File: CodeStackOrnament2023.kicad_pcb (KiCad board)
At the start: 2 copper layers, 68.8 x 68.8 mm, 26 parts, among them SW1 SW_SPST, U1 TLC555xD, U2 74VHC4040FT

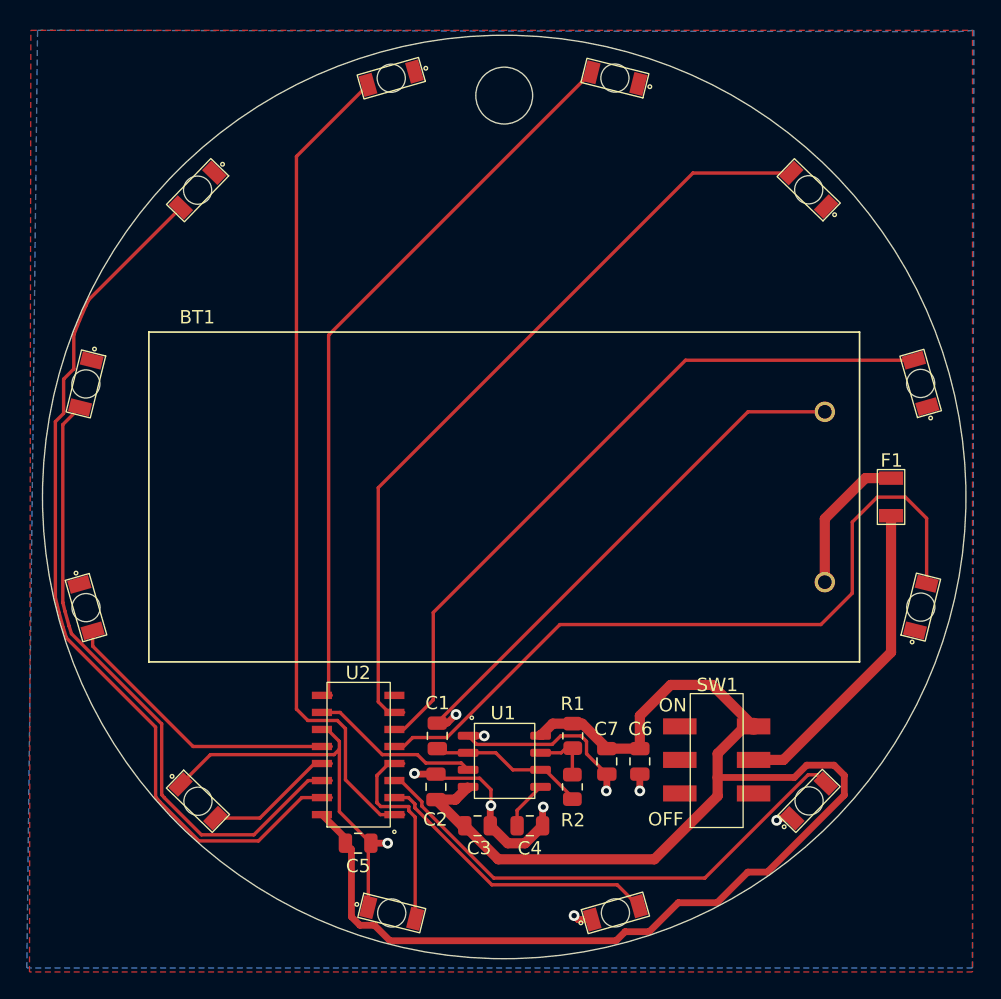
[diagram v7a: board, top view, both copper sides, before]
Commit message: increasing board size a bit.
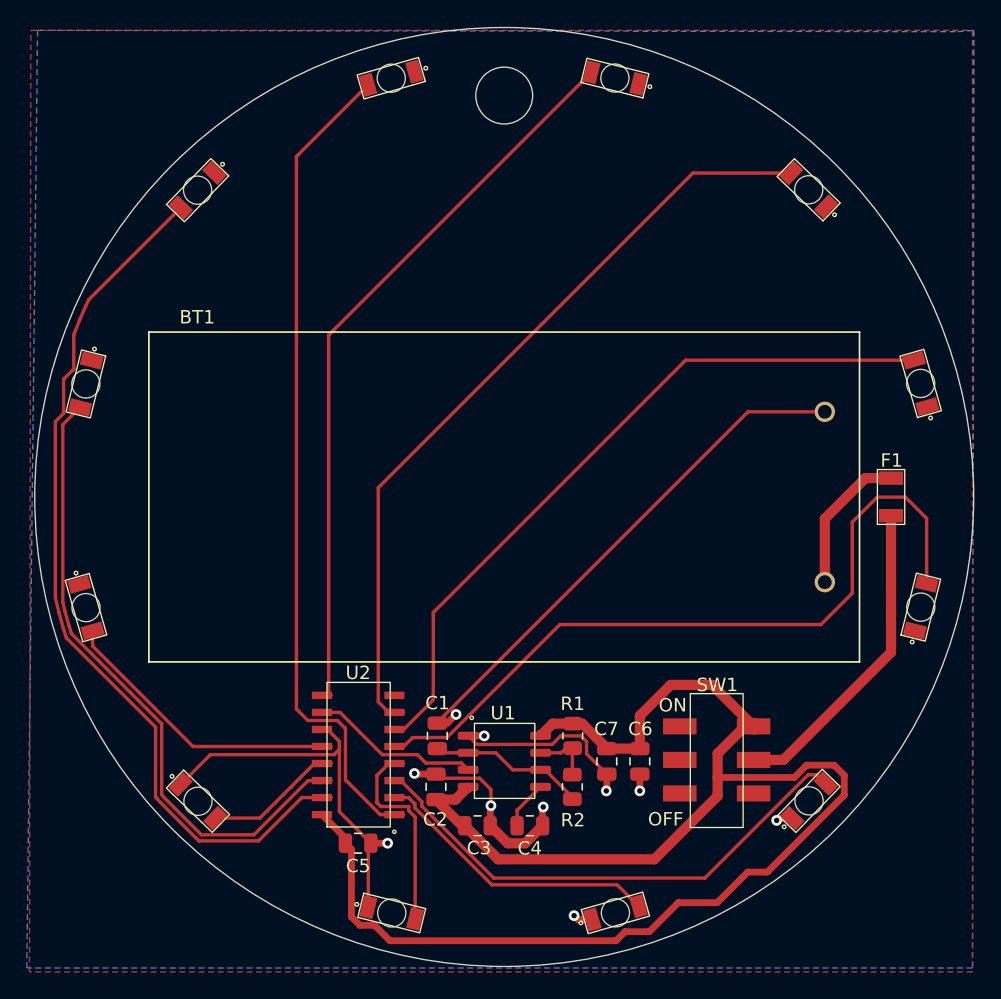
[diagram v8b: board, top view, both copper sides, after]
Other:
- board size 68.8 x 68.8 mm -> 70 x 70 mm
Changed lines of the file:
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@@
   (gr_circle (center 150.09 74.763659) (end 151.878206 75.900018)
     (stroke (width 0.1) (type default)) (fill none) (layer "Edge.Cuts"))
-  (gr_circle (center 150.09 104.688605) (end 163.752618 136.282363)
+  (gr_circle (center 150.09 104.688605) (end 185.09 104.688605)
     (stroke (width 0.1) (type default)) (fill none) (layer "Edge.Cuts"))
   (gr_text "OFF" (at 160.8 129.3) (layer "F.SilkS")
